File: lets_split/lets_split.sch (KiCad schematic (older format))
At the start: 55 parts, among them J2 CONN_01X04, P1 USB-rewire, P2 USB_OTG, SW1 SW_PUSH, SW10 SW_PUSH, SW11 SW_PUSH, SW12 SW_PUSH, SW13 SW_PUSH, SW14 SW_PUSH, SW15 SW_PUSH, SW16 SW_PUSH, SW17 SW_PUSH, SW18 SW_PUSH, SW19 SW_PUSH, SW2 SW_PUSH, SW20 SW_PUSH, SW21 SW_PUSH, SW22 SW_PUSH, SW23 SW_PUSH, SW24 SW_PUSH, SW3 SW_PUSH, SW4 SW_PUSH, SW5 SW_PUSH, SW6 SW_PUSH, SW7 SW_PUSH, SW8 SW_PUSH, SW9 SW_PUSH, U1 ArduinoProMicro

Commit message: Finished and panelized V3
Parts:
- added P3: WS2812-Strip, Wirepads:SMD_PAD_1x03_Pitch2.54mm, symbol CONN_01X03
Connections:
- net D+: now also P2.3 (D+); no longer P2.2 (D-)
- net D-: now also P2.2 (D-); no longer P2.3 (D+)
- net GND: now also P3.3 (P3)
- net VCC: now also P3.1 (P1)
- net col0: now also U1.20 (A3); no longer U1.9 (D6)
- net at U1.7 (D4): now also P3.2 (P2)
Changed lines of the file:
@@
 	1    0    0    -1
 $EndComp
-Text GLabel 2350 2375 2    55   Input ~ 0
+Text GLabel 2350 3475 2    55   Input ~ 0
 col0
 Text GLabel 2350 2675 2    55   Input ~ 0
@@
 $EndComp
 Wire Wire Line
-	5750 2500 6500 2500
-Wire Wire Line
-	6500 2500 7200 2500
-Wire Wire Line
-	7200 2500 7950 2500
-Wire Wire Line
-	7950 2500 8700 2500
-Wire Wire Line
-	8700 2500 9450 2500
+	5750 2500 9450 2500
 Connection ~ 8700 2500
 Connection ~ 7950 2500
@@
 Connection ~ 6500 2500
 Wire Wire Line
-	5750 3000 6500 3000
-Wire Wire Line
-	6500 3000 7200 3000
-Wire Wire Line
-	7200 3000 7950 3000
-Wire Wire Line
-	7950 3000 8700 3000
-Wire Wire Line
-	8700 3000 9450 3000
+	5750 3000 9450 3000
 Connection ~ 8700 3000
 Connection ~ 7950 3000
@@
 Connection ~ 6500 3000
 Wire Wire Line
-	5750 3500 6500 3500
-Wire Wire Line
-	6500 3500 7200 3500
-Wire Wire Line
-	7200 3500 7950 3500
-Wire Wire Line
-	7950 3500 8700 3500
-Wire Wire Line
-	8700 3500 9450 3500
+	5750 3500 9450 3500
 Connection ~ 8700 3500
 Connection ~ 7950 3500
@@
 Connection ~ 6500 3500
 Wire Wire Line
-	5750 4000 6500 4000
-Wire Wire Line
-	6500 4000 7200 4000
-Wire Wire Line
-	7200 4000 7950 4000
-Wire Wire Line
-	7950 4000 8700 4000
-Wire Wire Line
-	8700 4000 9450 4000
+	5750 4000 9450 4000
 Connection ~ 8700 4000
 Connection ~ 7950 4000
@@
 Connection ~ 6500 4000
 Wire Wire Line
-	5150 2200 5150 2700
-Wire Wire Line
-	5150 2700 5150 3200
-Wire Wire Line
-	5150 3200 5150 3700
+	5150 2200 5150 3700
 Connection ~ 5150 2700
 Connection ~ 5150 3200
 Wire Wire Line
-	5900 2200 5900 2700
-Wire Wire Line
-	5900 2700 5900 3200
-Wire Wire Line
-	5900 3200 5900 3700
+	5900 2200 5900 3700
 Connection ~ 5900 2700
 Connection ~ 5900 3200
 Wire Wire Line
-	6600 2200 6600 2700
-Wire Wire Line
-	6600 2700 6600 3200
-Wire Wire Line
-	6600 3200 6600 3700
+	6600 2200 6600 3700
 Connection ~ 6600 3200
 Connection ~ 6600 2700
 Wire Wire Line
-	7350 2200 7350 2700
-Wire Wire Line
-	7350 2700 7350 3200
-Wire Wire Line
-	7350 3200 7350 3700
+	7350 2200 7350 3700
 Connection ~ 7350 2700
 Connection ~ 7350 3200
 Wire Wire Line
-	8100 2200 8100 2700
-Wire Wire Line
-	8100 2700 8100 3200
-Wire Wire Line
-	8100 3200 8100 3700
+	8100 2200 8100 3700
 Connection ~ 8100 3200
 Connection ~ 8100 2700
 Wire Wire Line
-	8850 2200 8850 2700
-Wire Wire Line
-	8850 2700 8850 3200
-Wire Wire Line
-	8850 3200 8850 3700
+	8850 2200 8850 3700
 Connection ~ 8850 2700
 Connection ~ 8850 3200
@@
 	5850 1375 6375 1375
 Wire Wire Line
-	1400 2750 1400 2850
-Wire Wire Line
-	1400 2850 1400 2950
-Wire Wire Line
-	1400 2950 1400 3050
+	1400 2750 1400 3050
 Wire Wire Line
 	1400 2950 1550 2950
@@
 $EndComp
 Wire Wire Line
-	2350 2075 2750 2075
-Wire Wire Line
-	2750 2075 2850 2075
+	2350 2075 2850 2075
 Wire Wire Line
 	2750 2075 2750 1925
 Wire Wire Line
-	2350 1975 2650 1975
-Wire Wire Line
-	2650 1975 2850 1975
+	2350 1975 2850 1975
 Wire Wire Line
 	2650 1975 2650 1925
@@
 	2650 1725 2650 1675
 Wire Wire Line
-	2650 1675 2700 1675
-Wire Wire Line
-	2700 1675 2750 1675
+	2650 1675 2750 1675
 Wire Wire Line
 	2750 1675 2750 1725
@@
 	2225 4025 2275 4025
 Wire Wire Line
-	2275 4025 2275 4550
-Wire Wire Line
-	2275 4550 2275 4600
-Wire Wire Line
-	1925 4550 2025 4550
-Wire Wire Line
-	2025 4550 2275 4550
+	2275 4025 2275 4600
+Wire Wire Line
+	1925 4550 2275 4550
 Wire Wire Line
 	2025 4550 2025 4425
@@
 D+
 Wire Wire Line
-	1725 4500 1725 4775
-Wire Wire Line
-	1725 4500 1825 4500
-Wire Wire Line
-	1825 4500 1825 4425
-Wire Wire Line
-	1825 4550 1825 4775
-Wire Wire Line
-	1825 4550 1775 4550
-Wire Wire Line
-	1775 4550 1775 4450
-Wire Wire Line
-	1775 4450 1725 4450
-Wire Wire Line
-	1725 4450 1725 4425
+	1725 4425 1725 4775
+Wire Wire Line
+	1825 4425 1825 4775
+$Comp
+L CONN_01X03 P3
+U 1 1 59DDE6F8
+P 3575 2175
+F 0 "P3" H 3575 2375 50  0000 C CNN
+F 1 "WS2812-Strip" V 3675 2175 50  0000 C CNN
+F 2 "Wirepads:SMD_PAD_1x03_Pitch2.54mm" H 3575 2175 50  0001 C CNN
+F 3 "" H 3575 2175 50  0000 C CNN
+	1    3575 2175
+	1    0    0    -1
+$EndComp
+$Comp
+L VCC #PWR07
+U 1 1 59DDEE69
+P 3325 2025
+F 0 "#PWR07" H 3325 1875 50  0001 C CNN
+F 1 "VCC" H 3325 2175 50  0000 C CNN
+F 2 "" H 3325 2025 50  0000 C CNN
+F 3 "" H 3325 2025 50  0000 C CNN
+	1    3325 2025
+	1    0    0    -1
+$EndComp
+$Comp
+L GND #PWR08
+U 1 1 59DDF0E6
+P 3325 2325
+F 0 "#PWR08" H 3325 2075 50  0001 C CNN
+F 1 "GND" H 3325 2175 50  0000 C CNN
+F 2 "" H 3325 2325 50  0000 C CNN
+F 3 "" H 3325 2325 50  0000 C CNN
+	1    3325 2325
+	1    0    0    -1
+$EndComp
+Wire Wire Line
+	3325 2025 3325 2075
+Wire Wire Line
+	3325 2075 3375 2075
+Wire Wire Line
+	3325 2325 3325 2275
+Wire Wire Line
+	3325 2275 3375 2275
+Wire Wire Line
+	2350 2175 3375 2175
 $EndSCHEMATC

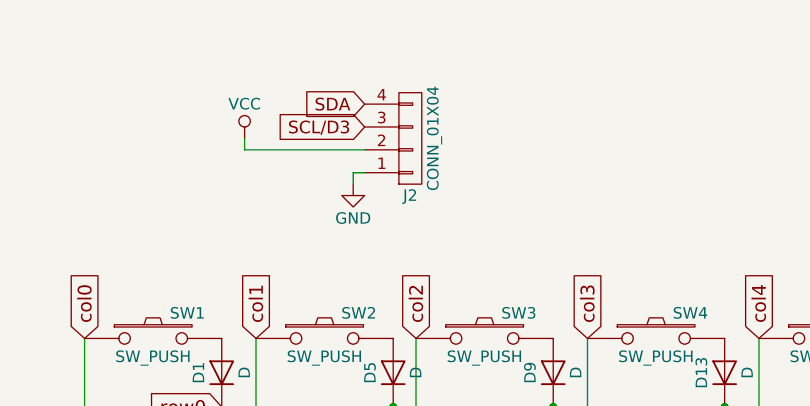
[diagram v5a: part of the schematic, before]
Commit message: Changed to actually aquireable TRRS connector
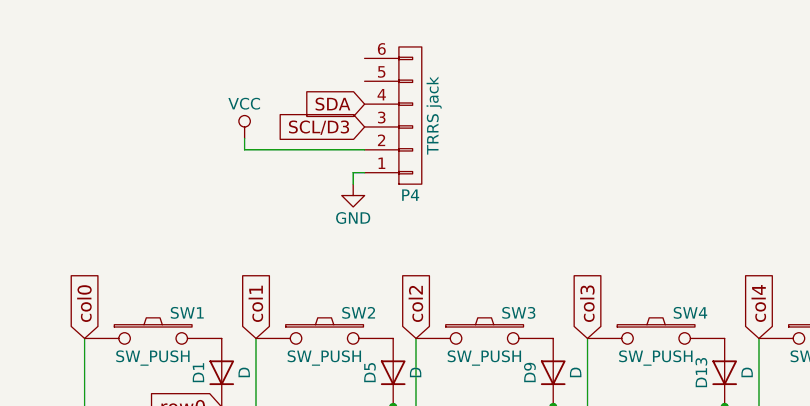
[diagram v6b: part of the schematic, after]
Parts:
- removed J2: CONN_01X04, Connectors:4ucon-20153, symbol CONN_01X04
- added P4: TRRS jack, Connectors:SJ-4351X-SMT, symbol CONN_01X06
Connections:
- net GND: now also P4.1 (P1)
- net SCL/D3: now also P4.3 (P3)
- net SDA: now also P4.4 (P4)
- net VCC: now also P4.2 (P2)
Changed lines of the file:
@@
 row3
-$Comp
-L CONN_01X04 J2
-U 1 1 59DC675D
-P 6575 1325
-F 0 "J2" H 6575 1575 50  0000 C CNN
-F 1 "CONN_01X04" V 6675 1325 50  0000 C CNN
-F 2 "Connectors:4ucon-20153" H 6575 1325 50  0001 C CNN
-F 3 "" H 6575 1325 50  0000 C CNN
-	1    6575 1325
-	1    0    0    1
-$EndComp
 $Comp
 L ArduinoProMicro U1
@@
 Wire Wire Line
 	2350 2175 3375 2175
+$Comp
+L CONN_01X06 P4
+U 1 1 59DEE7A5
+P 6575 1225
+F 0 "P4" H 6575 1575 50  0000 C CNN
+F 1 "TRRS jack" V 6675 1225 50  0000 C CNN
+F 2 "Connectors:SJ-4351X-SMT" H 6575 1225 50  0001 C CNN
+F 3 "" H 6575 1225 50  0000 C CNN
+	1    6575 1225
+	1    0    0    1
+$EndComp
 $EndSCHEMATC

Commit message: Switched to using diode footprints with actual silk screen, and moved dioes away from socket pads
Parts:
- D1, D10, D11, D12, D13, D14, D15, D16, D17, D18, D19, D2, D20, D21, D22, D23, D24, D3, D4, D5, D6, D7, D8, D9: footprint Diodes_ThroughHole:Diode_DO-41_SOD81_Horizontal_RM10 -> Diodes_ThroughHole:D_DO-41_SOD81_P7.62mm_Horizontal
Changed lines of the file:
@@
 F 0 "D1" H 5750 2450 50  0000 C CNN
 F 1 "D" H 5750 2250 50  0000 C CNN
-F 2 "Diodes_ThroughHole:Diode_DO-41_SOD81_Horizontal_RM10" H 5750 2350 50  0001 C CNN
+F 2 "Diodes_ThroughHole:D_DO-41_SOD81_P7.62mm_Horizontal" H 5750 2350 50  0001 C CNN
 F 3 "" H 5750 2350 50  0000 C CNN
 	1    5750 2350
@@
 F 0 "D5" H 6500 2450 50  0000 C CNN
 F 1 "D" H 6500 2250 50  0000 C CNN
-F 2 "Diodes_ThroughHole:Diode_DO-41_SOD81_Horizontal_RM10" H 6500 2350 50  0001 C CNN
+F 2 "Diodes_ThroughHole:D_DO-41_SOD81_P7.62mm_Horizontal" H 6500 2350 50  0001 C CNN
 F 3 "" H 6500 2350 50  0000 C CNN
 	1    6500 2350
@@
 F 0 "D9" H 7200 2450 50  0000 C CNN
 F 1 "D" H 7200 2250 50  0000 C CNN
-F 2 "Diodes_ThroughHole:Diode_DO-41_SOD81_Horizontal_RM10" H 7200 2350 50  0001 C CNN
+F 2 "Diodes_ThroughHole:D_DO-41_SOD81_P7.62mm_Horizontal" H 7200 2350 50  0001 C CNN
 F 3 "" H 7200 2350 50  0000 C CNN
 	1    7200 2350
@@
 F 0 "D13" H 7950 2450 50  0000 C CNN
 F 1 "D" H 7950 2250 50  0000 C CNN
-F 2 "Diodes_ThroughHole:Diode_DO-41_SOD81_Horizontal_RM10" H 7950 2350 50  0001 C CNN
+F 2 "Diodes_ThroughHole:D_DO-41_SOD81_P7.62mm_Horizontal" H 7950 2350 50  0001 C CNN
 F 3 "" H 7950 2350 50  0000 C CNN
 	1    7950 2350
@@
 F 0 "D17" H 8700 2450 50  0000 C CNN
 F 1 "D" H 8700 2250 50  0000 C CNN
-F 2 "Diodes_ThroughHole:Diode_DO-41_SOD81_Horizontal_RM10" H 8700 2350 50  0001 C CNN
+F 2 "Diodes_ThroughHole:D_DO-41_SOD81_P7.62mm_Horizontal" H 8700 2350 50  0001 C CNN
 F 3 "" H 8700 2350 50  0000 C CNN
 	1    8700 2350
@@
 F 0 "D21" H 9450 2450 50  0000 C CNN
 F 1 "D" H 9450 2250 50  0000 C CNN
-F 2 "Diodes_ThroughHole:Diode_DO-41_SOD81_Horizontal_RM10" H 9450 2350 50  0001 C CNN
+F 2 "Diodes_ThroughHole:D_DO-41_SOD81_P7.62mm_Horizontal" H 9450 2350 50  0001 C CNN
 F 3 "" H 9450 2350 50  0000 C CNN
 	1    9450 2350
@@
 F 0 "D2" H 5750 2950 50  0000 C CNN
 F 1 "D" H 5750 2750 50  0000 C CNN
-F 2 "Diodes_ThroughHole:Diode_DO-41_SOD81_Horizontal_RM10" H 5750 2850 50  0001 C CNN
+F 2 "Diodes_ThroughHole:D_DO-41_SOD81_P7.62mm_Horizontal" H 5750 2850 50  0001 C CNN
 F 3 "" H 5750 2850 50  0000 C CNN
 	1    5750 2850
@@
 F 0 "D6" H 6500 2950 50  0000 C CNN
 F 1 "D" H 6500 2750 50  0000 C CNN
-F 2 "Diodes_ThroughHole:Diode_DO-41_SOD81_Horizontal_RM10" H 6500 2850 50  0001 C CNN
+F 2 "Diodes_ThroughHole:D_DO-41_SOD81_P7.62mm_Horizontal" H 6500 2850 50  0001 C CNN
 F 3 "" H 6500 2850 50  0000 C CNN
 	1    6500 2850
@@
 F 0 "D10" H 7200 2950 50  0000 C CNN
 F 1 "D" H 7200 2750 50  0000 C CNN
-F 2 "Diodes_ThroughHole:Diode_DO-41_SOD81_Horizontal_RM10" H 7200 2850 50  0001 C CNN
+F 2 "Diodes_ThroughHole:D_DO-41_SOD81_P7.62mm_Horizontal" H 7200 2850 50  0001 C CNN
 F 3 "" H 7200 2850 50  0000 C CNN
 	1    7200 2850
@@
 F 0 "D14" H 7950 2950 50  0000 C CNN
 F 1 "D" H 7950 2750 50  0000 C CNN
-F 2 "Diodes_ThroughHole:Diode_DO-41_SOD81_Horizontal_RM10" H 7950 2850 50  0001 C CNN
+F 2 "Diodes_ThroughHole:D_DO-41_SOD81_P7.62mm_Horizontal" H 7950 2850 50  0001 C CNN
 F 3 "" H 7950 2850 50  0000 C CNN
 	1    7950 2850
@@
 F 0 "D18" H 8700 2950 50  0000 C CNN
 F 1 "D" H 8700 2750 50  0000 C CNN
-F 2 "Diodes_ThroughHole:Diode_DO-41_SOD81_Horizontal_RM10" H 8700 2850 50  0001 C CNN
+F 2 "Diodes_ThroughHole:D_DO-41_SOD81_P7.62mm_Horizontal" H 8700 2850 50  0001 C CNN
 F 3 "" H 8700 2850 50  0000 C CNN
 	1    8700 2850
@@
 F 0 "D22" H 9450 2950 50  0000 C CNN
 F 1 "D" H 9450 2750 50  0000 C CNN
-F 2 "Diodes_ThroughHole:Diode_DO-41_SOD81_Horizontal_RM10" H 9450 2850 50  0001 C CNN
+F 2 "Diodes_ThroughHole:D_DO-41_SOD81_P7.62mm_Horizontal" H 9450 2850 50  0001 C CNN
 F 3 "" H 9450 2850 50  0000 C CNN
 	1    9450 2850
@@
 F 0 "D3" H 5750 3450 50  0000 C CNN
 F 1 "D" H 5750 3250 50  0000 C CNN
-F 2 "Diodes_ThroughHole:Diode_DO-41_SOD81_Horizontal_RM10" H 5750 3350 50  0001 C CNN
+F 2 "Diodes_ThroughHole:D_DO-41_SOD81_P7.62mm_Horizontal" H 5750 3350 50  0001 C CNN
 F 3 "" H 5750 3350 50  0000 C CNN
 	1    5750 3350
@@
 F 0 "D7" H 6500 3450 50  0000 C CNN
 F 1 "D" H 6500 3250 50  0000 C CNN
-F 2 "Diodes_ThroughHole:Diode_DO-41_SOD81_Horizontal_RM10" H 6500 3350 50  0001 C CNN
+F 2 "Diodes_ThroughHole:D_DO-41_SOD81_P7.62mm_Horizontal" H 6500 3350 50  0001 C CNN
 F 3 "" H 6500 3350 50  0000 C CNN
 	1    6500 3350
@@
 F 0 "D11" H 7200 3450 50  0000 C CNN
 F 1 "D" H 7200 3250 50  0000 C CNN
-F 2 "Diodes_ThroughHole:Diode_DO-41_SOD81_Horizontal_RM10" H 7200 3350 50  0001 C CNN
+F 2 "Diodes_ThroughHole:D_DO-41_SOD81_P7.62mm_Horizontal" H 7200 3350 50  0001 C CNN
 F 3 "" H 7200 3350 50  0000 C CNN
 	1    7200 3350
@@
 F 0 "D15" H 7950 3450 50  0000 C CNN
 F 1 "D" H 7950 3250 50  0000 C CNN
-F 2 "Diodes_ThroughHole:Diode_DO-41_SOD81_Horizontal_RM10" H 7950 3350 50  0001 C CNN
+F 2 "Diodes_ThroughHole:D_DO-41_SOD81_P7.62mm_Horizontal" H 7950 3350 50  0001 C CNN
 F 3 "" H 7950 3350 50  0000 C CNN
 	1    7950 3350
@@
 F 0 "D19" H 8700 3450 50  0000 C CNN
 F 1 "D" H 8700 3250 50  0000 C CNN
-F 2 "Diodes_ThroughHole:Diode_DO-41_SOD81_Horizontal_RM10" H 8700 3350 50  0001 C CNN
+F 2 "Diodes_ThroughHole:D_DO-41_SOD81_P7.62mm_Horizontal" H 8700 3350 50  0001 C CNN
 F 3 "" H 8700 3350 50  0000 C CNN
 	1    8700 3350
@@
 F 0 "D23" H 9450 3450 50  0000 C CNN
 F 1 "D" H 9450 3250 50  0000 C CNN
-F 2 "Diodes_ThroughHole:Diode_DO-41_SOD81_Horizontal_RM10" H 9450 3350 50  0001 C CNN
+F 2 "Diodes_ThroughHole:D_DO-41_SOD81_P7.62mm_Horizontal" H 9450 3350 50  0001 C CNN
 F 3 "" H 9450 3350 50  0000 C CNN
 	1    9450 3350
@@
 F 0 "D4" H 5750 3950 50  0000 C CNN
 F 1 "D" H 5750 3750 50  0000 C CNN
-F 2 "Diodes_ThroughHole:Diode_DO-41_SOD81_Horizontal_RM10" H 5750 3850 50  0001 C CNN
+F 2 "Diodes_ThroughHole:D_DO-41_SOD81_P7.62mm_Horizontal" H 5750 3850 50  0001 C CNN
 F 3 "" H 5750 3850 50  0000 C CNN
 	1    5750 3850
@@
 F 0 "D8" H 6500 3950 50  0000 C CNN
 F 1 "D" H 6500 3750 50  0000 C CNN
-F 2 "Diodes_ThroughHole:Diode_DO-41_SOD81_Horizontal_RM10" H 6500 3850 50  0001 C CNN
+F 2 "Diodes_ThroughHole:D_DO-41_SOD81_P7.62mm_Horizontal" H 6500 3850 50  0001 C CNN
 F 3 "" H 6500 3850 50  0000 C CNN
 	1    6500 3850
@@
 F 0 "D12" H 7200 3950 50  0000 C CNN
 F 1 "D" H 7200 3750 50  0000 C CNN
-F 2 "Diodes_ThroughHole:Diode_DO-41_SOD81_Horizontal_RM10" H 7200 3850 50  0001 C CNN
+F 2 "Diodes_ThroughHole:D_DO-41_SOD81_P7.62mm_Horizontal" H 7200 3850 50  0001 C CNN
 F 3 "" H 7200 3850 50  0000 C CNN
 	1    7200 3850
@@
 F 0 "D16" H 7950 3950 50  0000 C CNN
 F 1 "D" H 7950 3750 50  0000 C CNN
-F 2 "Diodes_ThroughHole:Diode_DO-41_SOD81_Horizontal_RM10" H 7950 3850 50  0001 C CNN
+F 2 "Diodes_ThroughHole:D_DO-41_SOD81_P7.62mm_Horizontal" H 7950 3850 50  0001 C CNN
 F 3 "" H 7950 3850 50  0000 C CNN
 	1    7950 3850
@@
 F 0 "D20" H 8700 3950 50  0000 C CNN
 F 1 "D" H 8700 3750 50  0000 C CNN
-F 2 "Diodes_ThroughHole:Diode_DO-41_SOD81_Horizontal_RM10" H 8700 3850 50  0001 C CNN
+F 2 "Diodes_ThroughHole:D_DO-41_SOD81_P7.62mm_Horizontal" H 8700 3850 50  0001 C CNN
 F 3 "" H 8700 3850 50  0000 C CNN
 	1    8700 3850
@@
 F 0 "D24" H 9450 3950 50  0000 C CNN
 F 1 "D" H 9450 3750 50  0000 C CNN
-F 2 "Diodes_ThroughHole:Diode_DO-41_SOD81_Horizontal_RM10" H 9450 3850 50  0001 C CNN
+F 2 "Diodes_ThroughHole:D_DO-41_SOD81_P7.62mm_Horizontal" H 9450 3850 50  0001 C CNN
 F 3 "" H 9450 3850 50  0000 C CNN
 	1    9450 3850
